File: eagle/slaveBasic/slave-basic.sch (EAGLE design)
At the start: 26 parts, among them CON2 SPI, CON3 SPI, IC3 MCP1703CB, J1 RJ12RIGHTANGLE-I2C, J2 RJ12RIGHTANGLE-I2C, U3 ATMEGA328

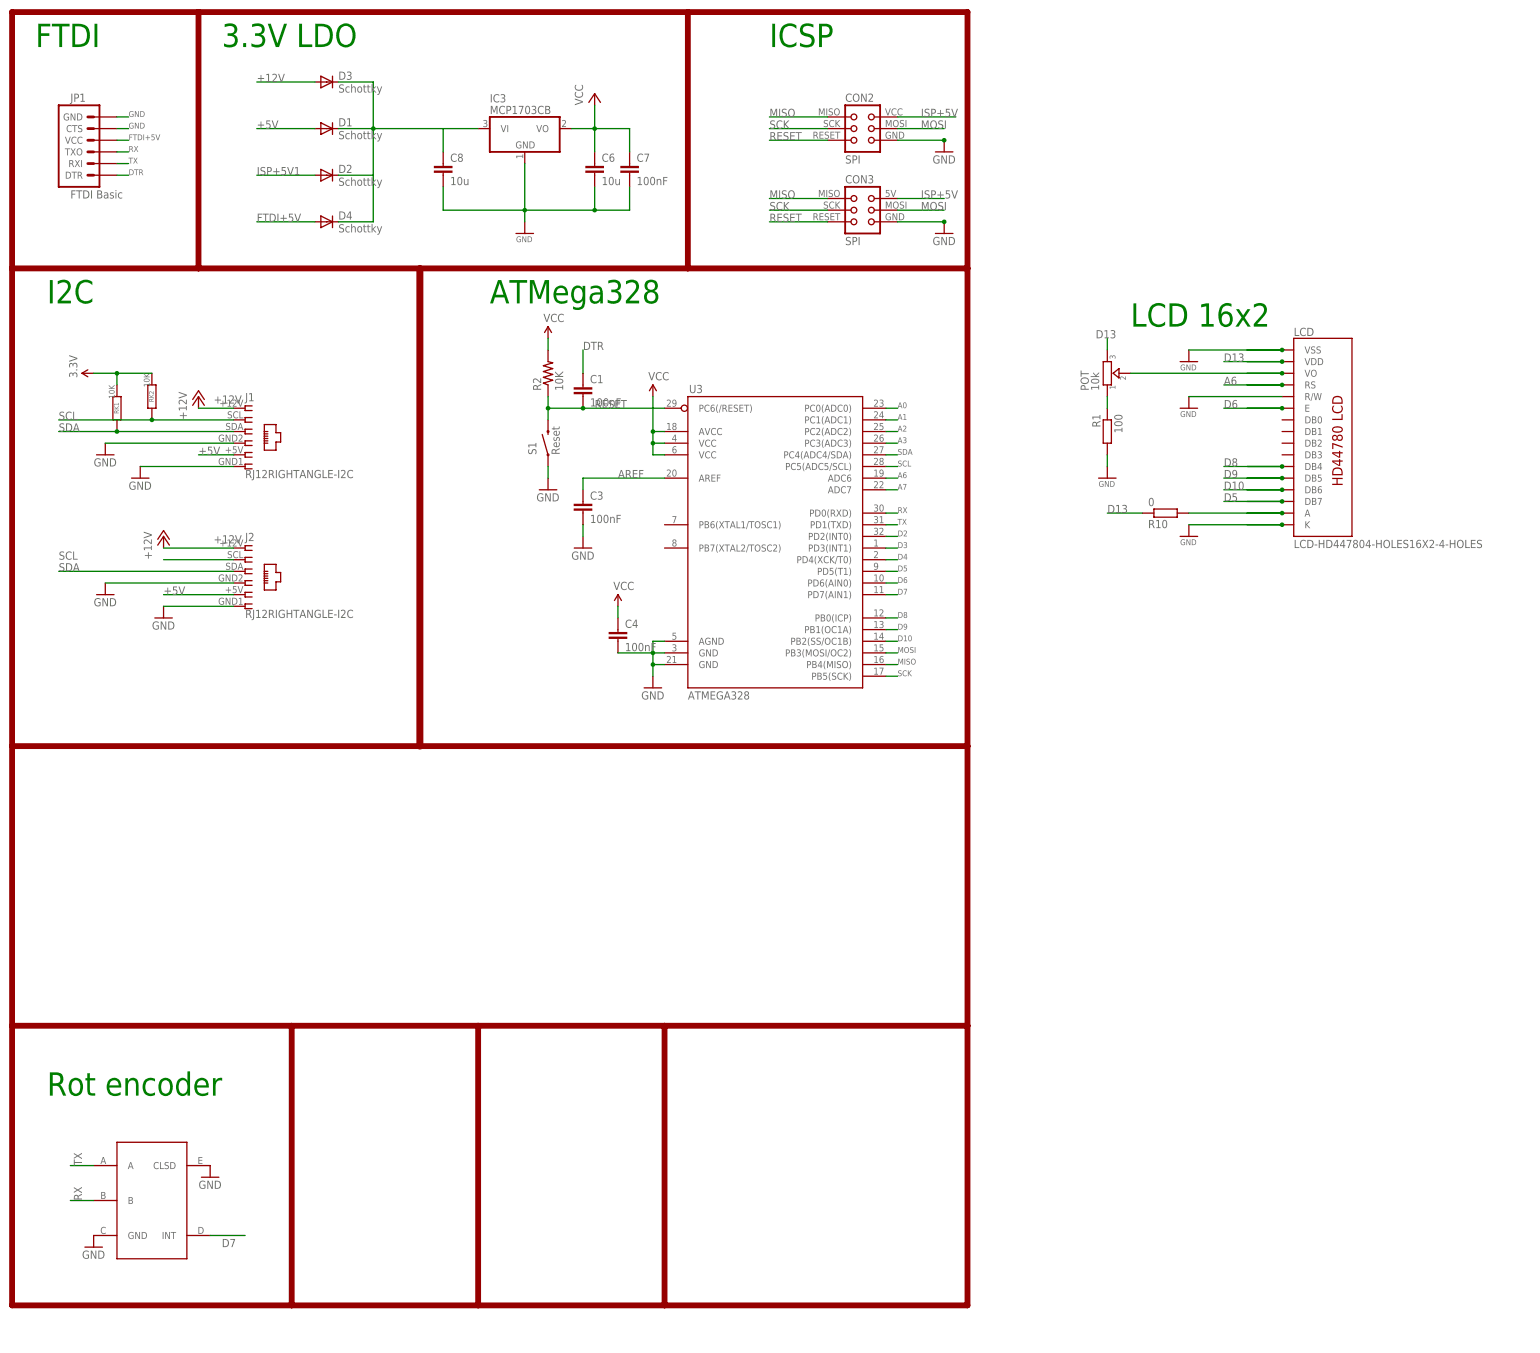
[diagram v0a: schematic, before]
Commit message: create slaves-i2c folder
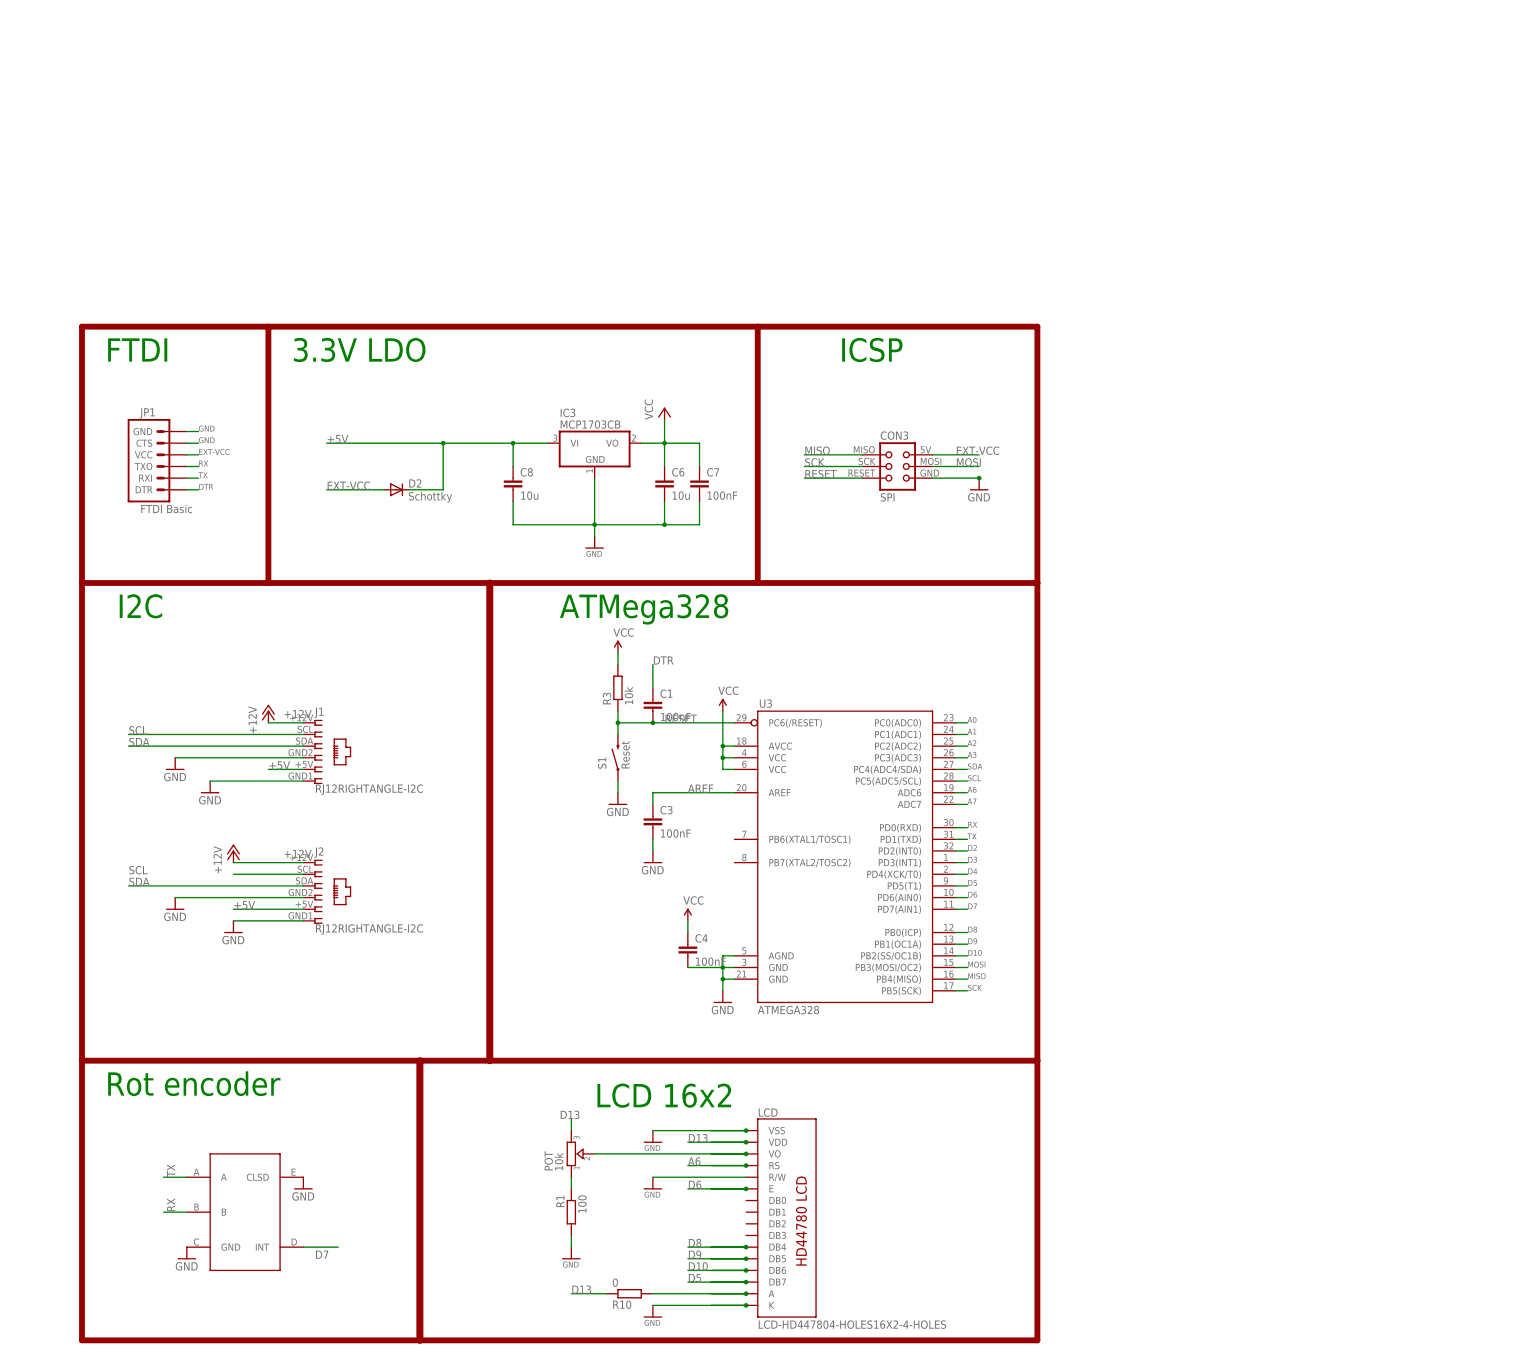
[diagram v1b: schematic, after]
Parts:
- removed CON2: SPI, lpatiny:TINYISP
- removed D1, D3, D4: Schottky, diode:MBR0520LT
- removed R2: 10K, SparkFun:RESISTOR0603-RES
- removed RK1, RK2: 10K, resistor:R-EU_M0805
- added R3: 10k, rcl:R-EU_R0805
- CON3: device lpatiny:TINYISPT -> lpatiny:TINYISPTAG
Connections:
- removed net 3.3V: C4.1, RK1.1, RK2.1
- removed net FTDI+5V: D4.A, JP1.VCC
- removed net ISP+5V: CON2.VCC, CON3.VCC
- removed net ISP+5V1: D2.A
- removed net N$1: C8.1, IC3.VI
- removed net N$3: D1.C, D2.C, D3.C, D4.C
- new net EXT-VCC: CON3.VCC, D2.A, JP1.VCC
- net +12V: no longer D3.A
- net +5V: now also C8.1, D2.C, IC3.VI; no longer D1.A
- net GND: no longer CON2.GND
- net MISO: no longer CON2.MISO
- net MOSI: no longer CON2.MOSI
- net RESET: now also R3.1; no longer CON2.RESET, R2.1
- net SCK: no longer CON2.SCK
- net SCL: no longer RK2.2
- net SDA: no longer RK1.2
- net VCC: now also C4.1, R3.2; no longer R2.2
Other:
- moved on the sheet: C1, C3, C4, C6, C7, C8, CON3, D2, IC3, J1, J2, JP1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
